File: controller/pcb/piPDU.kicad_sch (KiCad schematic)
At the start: 36 parts, among them J0 SCR_BTN1, J1 SCR_LED1, J10 SCR_BTN6, J11 SCR_LED6, J12 SCR_BTN7, J13 SCR_LED7, J14 SCR_BTN8, J15 SCR_LED8, J16 SCR_BTN9, J17 SCR_LED9, J18 SCR_BTN10, J19 SCR_LED10, J2 SCR_BTN2, J20 SCR_BTN11, J21 SCR_LED11, J22 SCR_BTN12, J23 SCR_LED12, J24 SCR_BTN13, J25 SCR_LED13, J26 SCR_BTN14, J27 SCR_LED14, J28 SCR_BTN15, J29 SCR_LED15, J3 SCR_LED2, J30 SCR_BTN16, J31 SCR_LED16, J32 SCR_5V, J33 SCR_LCD_PWR, J34 SCR_LCD_DATA, J35 Raspberry_Pi_2_3, J4 SCR_BTN3, J5 SCR_LED3, J6 SCR_BTN4, J7 SCR_LED4, J8 SCR_BTN5, J9 SCR_LED5

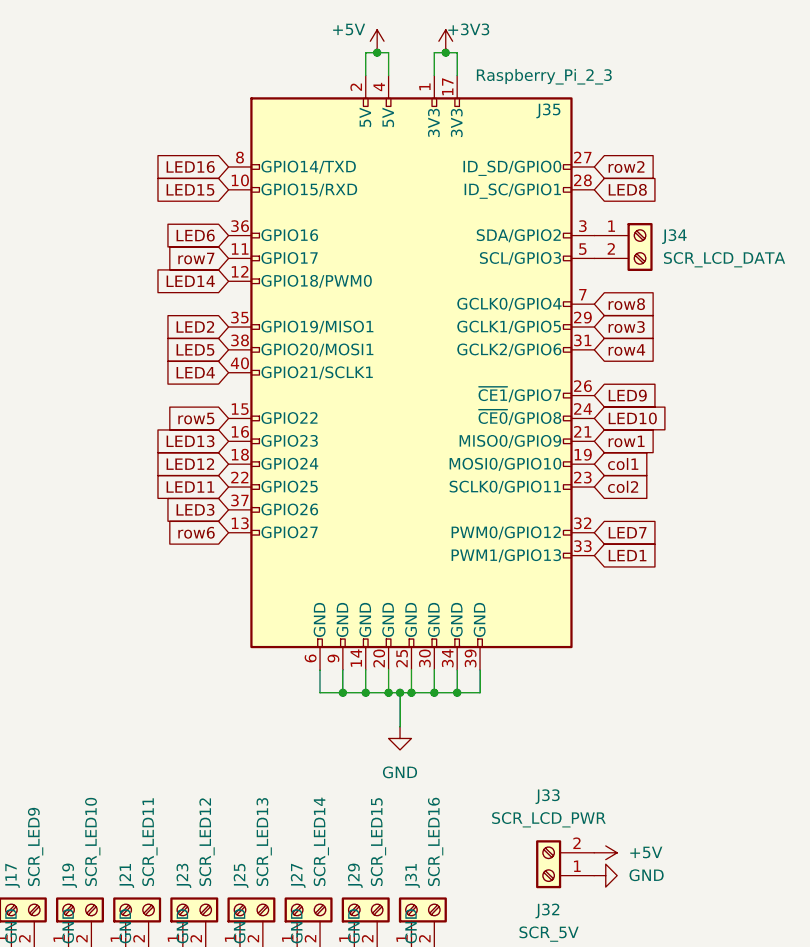
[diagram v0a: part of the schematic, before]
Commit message: Remove redundant connections from the schematic
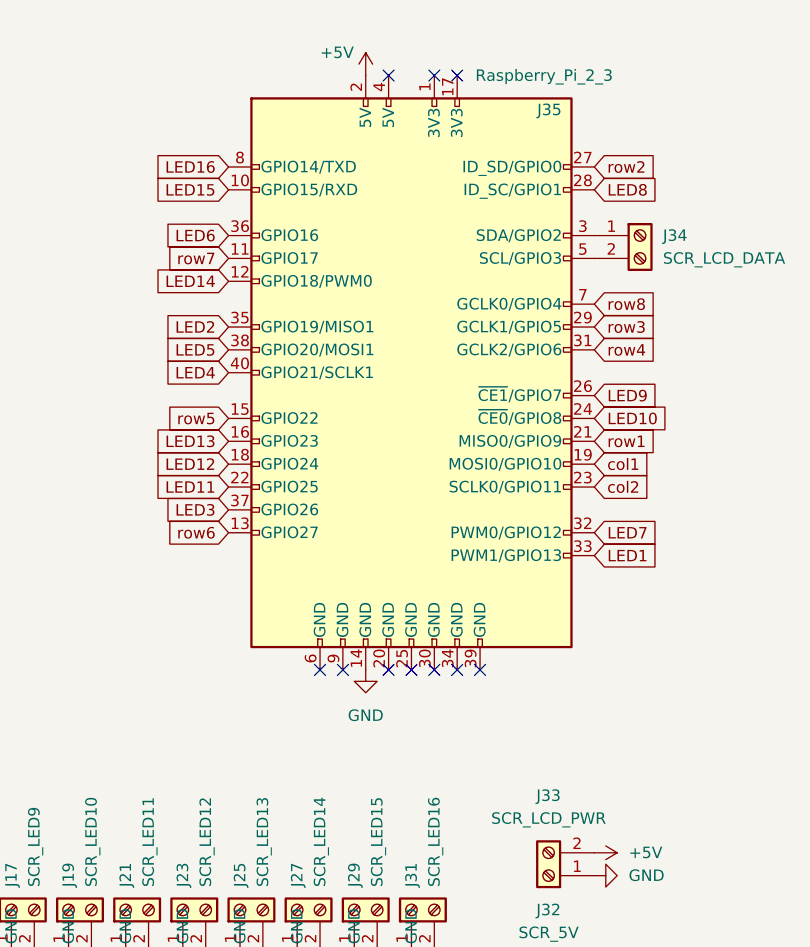
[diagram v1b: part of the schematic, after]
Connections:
- net +5V: no longer J35.4 (5V)
- net GND: no longer J35.20 (GND), J35.25 (GND), J35.30 (GND), J35.34 (GND), J35.39 (GND), J35.6 (GND), J35.9 (GND)
- net +3V3: no longer names the net of J35.1 (3V3)
- net +3V3: no longer J35.17 (3V3)
- no-connect marks 0 -> 10
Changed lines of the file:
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@@
   (junction (at 55.88 69.85) (diameter 0) (color 0 0 0 0)
   )
-  (junction (at 113.03 88.9) (diameter 0) (color 0 0 0 0)
-  )
-  (junction (at 109.22 17.78) (diameter 0) (color 0 0 0 0)
-  )
   (junction (at 55.88 39.37) (diameter 0) (color 0 0 0 0)
   )
-  (junction (at 110.49 88.9) (diameter 0) (color 0 0 0 0)
-  )
-  (junction (at 107.95 88.9) (diameter 0) (color 0 0 0 0)
-  )
-  (junction (at 111.76 88.9) (diameter 0) (color 0 0 0 0)
-  )
   (junction (at 55.88 54.61) (diameter 0) (color 0 0 0 0)
   )
@@
   (junction (at 36.83 77.47) (diameter 0) (color 0 0 0 0)
   )
-  (junction (at 105.41 88.9) (diameter 0) (color 0 0 0 0)
-  )
   (junction (at 54.61 58.42) (diameter 0) (color 0 0 0 0)
   )
   (junction (at 36.83 31.75) (diameter 0) (color 0 0 0 0)
   )
-  (junction (at 115.57 88.9) (diameter 0) (color 0 0 0 0)
-  )
-  (junction (at 116.84 17.78) (diameter 0) (color 0 0 0 0)
-  )
-  (junction (at 118.11 88.9) (diameter 0) (color 0 0 0 0)
-  )
+  (no_connect (at 105.41 86.36))
+  (no_connect (at 118.11 20.32))
+  (no_connect (at 118.11 86.36))
+  (no_connect (at 120.65 86.36))
+  (no_connect (at 115.57 20.32))
+  (no_connect (at 113.03 86.36))
+  (no_connect (at 110.49 86.36))
+  (no_connect (at 115.57 86.36))
+  (no_connect (at 102.87 86.36))
+  (no_connect (at 110.49 20.32))
   (wire (pts (xy 54.61 50.8) (xy 54.61 49.53))
     (stroke (width 0) (type default) (color 0 0 0 0))
@@
     (stroke (width 0) (type default) (color 0 0 0 0))
   )
-  (wire (pts (xy 102.87 86.36) (xy 102.87 88.9))
-    (stroke (width 0) (type default) (color 0 0 0 0))
-  )
-  (wire (pts (xy 115.57 20.32) (xy 115.57 17.78))
-    (stroke (width 0) (type default) (color 0 0 0 0))
-  )
   (wire (pts (xy 36.83 69.85) (xy 35.56 69.85))
     (stroke (width 0) (type default) (color 0 0 0 0))
   )
-  (wire (pts (xy 107.95 17.78) (xy 107.95 20.32))
-    (stroke (width 0) (type default) (color 0 0 0 0))
-  )
-  (wire (pts (xy 115.57 17.78) (xy 116.84 17.78))
-    (stroke (width 0) (type default) (color 0 0 0 0))
-  )
-  (wire (pts (xy 111.76 88.9) (xy 113.03 88.9))
-    (stroke (width 0) (type default) (color 0 0 0 0))
-  )
   (wire (pts (xy 36.83 46.99) (xy 36.83 54.61))
     (stroke (width 0) (type default) (color 0 0 0 0))
   )
-  (wire (pts (xy 107.95 88.9) (xy 110.49 88.9))
-    (stroke (width 0) (type default) (color 0 0 0 0))
-  )
   (wire (pts (xy 57.15 24.13) (xy 55.88 24.13))
     (stroke (width 0) (type default) (color 0 0 0 0))
@@
     (stroke (width 0) (type default) (color 0 0 0 0))
   )
-  (wire (pts (xy 107.95 86.36) (xy 107.95 88.9))
-    (stroke (width 0) (type default) (color 0 0 0 0))
-  )
   (wire (pts (xy 36.83 39.37) (xy 35.56 39.37))
     (stroke (width 0) (type default) (color 0 0 0 0))
@@
     (stroke (width 0) (type default) (color 0 0 0 0))
   )
-  (wire (pts (xy 113.03 86.36) (xy 113.03 88.9))
-    (stroke (width 0) (type default) (color 0 0 0 0))
-  )
-  (wire (pts (xy 118.11 86.36) (xy 118.11 88.9))
-    (stroke (width 0) (type default) (color 0 0 0 0))
-  )
   (wire (pts (xy 54.61 73.66) (xy 58.42 73.66))
     (stroke (width 0) (type default) (color 0 0 0 0))
   )
-  (wire (pts (xy 111.76 88.9) (xy 110.49 88.9))
-    (stroke (width 0) (type default) (color 0 0 0 0))
-  )
   (wire (pts (xy 35.56 87.63) (xy 35.56 90.17))
     (stroke (width 0) (type default) (color 0 0 0 0))
@@
     (stroke (width 0) (type default) (color 0 0 0 0))
   )
-  (wire (pts (xy 118.11 17.78) (xy 118.11 20.32))
-    (stroke (width 0) (type default) (color 0 0 0 0))
-  )
   (wire (pts (xy 55.88 24.13) (xy 55.88 31.75))
     (stroke (width 0) (type default) (color 0 0 0 0))
@@
     (stroke (width 0) (type default) (color 0 0 0 0))
   )
-  (wire (pts (xy 118.11 88.9) (xy 120.65 88.9))
-    (stroke (width 0) (type default) (color 0 0 0 0))
-  )
   (wire (pts (xy 35.56 34.29) (xy 35.56 36.83))
     (stroke (width 0) (type default) (color 0 0 0 0))
   )
-  (wire (pts (xy 105.41 86.36) (xy 105.41 88.9))
-    (stroke (width 0) (type default) (color 0 0 0 0))
-  )
   (wire (pts (xy 35.56 36.83) (xy 54.61 36.83))
     (stroke (width 0) (type default) (color 0 0 0 0))
@@
     (stroke (width 0) (type default) (color 0 0 0 0))
   )
-  (wire (pts (xy 110.49 86.36) (xy 110.49 88.9))
-    (stroke (width 0) (type default) (color 0 0 0 0))
-  )
-  (wire (pts (xy 111.76 92.71) (xy 111.76 88.9))
-    (stroke (width 0) (type default) (color 0 0 0 0))
-  )
   (wire (pts (xy 36.83 31.75) (xy 36.83 39.37))
     (stroke (width 0) (type default) (color 0 0 0 0))
@@
     (stroke (width 0) (type default) (color 0 0 0 0))
   )
-  (wire (pts (xy 115.57 86.36) (xy 115.57 88.9))
-    (stroke (width 0) (type default) (color 0 0 0 0))
-  )
   (wire (pts (xy 35.56 74.93) (xy 54.61 74.93))
     (stroke (width 0) (type default) (color 0 0 0 0))
@@
     (stroke (width 0) (type default) (color 0 0 0 0))
   )
-  (wire (pts (xy 110.49 20.32) (xy 110.49 17.78))
-    (stroke (width 0) (type default) (color 0 0 0 0))
-  )
   (wire (pts (xy 35.56 80.01) (xy 35.56 82.55))
     (stroke (width 0) (type default) (color 0 0 0 0))
@@
     (stroke (width 0) (type default) (color 0 0 0 0))
   )
-  (wire (pts (xy 110.49 17.78) (xy 109.22 17.78))
-    (stroke (width 0) (type default) (color 0 0 0 0))
-  )
   (wire (pts (xy 55.88 77.47) (xy 55.88 85.09))
     (stroke (width 0) (type default) (color 0 0 0 0))
@@
     (stroke (width 0) (type default) (color 0 0 0 0))
   )
-  (wire (pts (xy 116.84 17.78) (xy 118.11 17.78))
-    (stroke (width 0) (type default) (color 0 0 0 0))
-  )
   (wire (pts (xy 36.83 85.09) (xy 35.56 85.09))
     (stroke (width 0) (type default) (color 0 0 0 0))
@@
     (stroke (width 0) (type default) (color 0 0 0 0))
   )
-  (wire (pts (xy 113.03 88.9) (xy 115.57 88.9))
-    (stroke (width 0) (type default) (color 0 0 0 0))
-  )
   (wire (pts (xy 54.61 67.31) (xy 54.61 66.04))
     (stroke (width 0) (type default) (color 0 0 0 0))
@@
     (stroke (width 0) (type default) (color 0 0 0 0))
   )
-  (wire (pts (xy 109.22 17.78) (xy 107.95 17.78))
-    (stroke (width 0) (type default) (color 0 0 0 0))
-  )
   (wire (pts (xy 54.61 77.47) (xy 55.88 77.47))
     (stroke (width 0) (type default) (color 0 0 0 0))
@@
     (stroke (width 0) (type default) (color 0 0 0 0))
   )
-  (wire (pts (xy 120.65 88.9) (xy 120.65 86.36))
-    (stroke (width 0) (type default) (color 0 0 0 0))
-  )
-  (wire (pts (xy 115.57 88.9) (xy 118.11 88.9))
-    (stroke (width 0) (type default) (color 0 0 0 0))
-  )
   (wire (pts (xy 35.56 41.91) (xy 35.56 44.45))
     (stroke (width 0) (type default) (color 0 0 0 0))
@@
     (stroke (width 0) (type default) (color 0 0 0 0))
   )
-  (wire (pts (xy 102.87 88.9) (xy 105.41 88.9))
-    (stroke (width 0) (type default) (color 0 0 0 0))
-  )
   (wire (pts (xy 35.56 57.15) (xy 35.56 59.69))
     (stroke (width 0) (type default) (color 0 0 0 0))
   )
-  (wire (pts (xy 105.41 88.9) (xy 107.95 88.9))
-    (stroke (width 0) (type default) (color 0 0 0 0))
-  )
   (global_label "row5" (shape input) (at 92.71 58.42 180) (fields_autoplaced)
     (effects (font (size 1.27 1.27)) (justify right))
@@
     (pin "2")
   )
-  (symbol (lib_id "power:+5V") (at 109.22 17.78 0) (unit 1)
+  (symbol (lib_id "power:+5V") (at 107.95 20.32 0) (unit 1)
     (in_bom yes) (on_board yes)
-    (property "Reference" "#PWR0121" (id 0) (at 109.22 21.59 0)
-      (effects (font (size 1.27 1.27)) hide)
-    )
-    (property "Value" "+5V" (id 1) (at 104.14 15.24 0)
-      (effects (font (size 1.27 1.27)) (justify left))
-    )
-    (property "Footprint" "" (id 2) (at 109.22 17.78 0)
-      (effects (font (size 1.27 1.27)) hide)
-    )
-    (property "Datasheet" "" (id 3) (at 109.22 17.78 0)
+    (property "Reference" "#PWR0121" (id 0) (at 107.95 24.13 0)
+      (effects (font (size 1.27 1.27)) hide)
+    )
+    (property "Value" "+5V" (id 1) (at 102.87 17.78 0)
+      (effects (font (size 1.27 1.27)) (justify left))
+    )
+    (property "Footprint" "" (id 2) (at 107.95 20.32 0)
+      (effects (font (size 1.27 1.27)) hide)
+    )
+    (property "Datasheet" "" (id 3) (at 107.95 20.32 0)
       (effects (font (size 1.27 1.27)) hide)
     )
@@
     (pin "2")
   )
-  (symbol (lib_id "power:GND") (at 111.76 92.71 0) (unit 1)
-    (in_bom yes) (on_board yes) (fields_autoplaced)
-    (property "Reference" "#PWR0103" (id 0) (at 111.76 99.06 0)
-      (effects (font (size 1.27 1.27)) hide)
-    )
-    (property "Value" "GND" (id 1) (at 111.76 97.79 0))
-    (property "Footprint" "" (id 2) (at 111.76 92.71 0)
-      (effects (font (size 1.27 1.27)) hide)
-    )
-    (property "Datasheet" "" (id 3) (at 111.76 92.71 0)
+  (symbol (lib_id "power:GND") (at 107.95 86.36 0) (unit 1)
+    (in_bom yes) (on_board yes) (fields_autoplaced)
+    (property "Reference" "#PWR0103" (id 0) (at 107.95 92.71 0)
+      (effects (font (size 1.27 1.27)) hide)
+    )
+    (property "Value" "GND" (id 1) (at 107.95 91.44 0))
+    (property "Footprint" "" (id 2) (at 107.95 86.36 0)
+      (effects (font (size 1.27 1.27)) hide)
+    )
+    (property "Datasheet" "" (id 3) (at 107.95 86.36 0)
       (effects (font (size 1.27 1.27)) hide)
     )
@@
     (pin "1")
     (pin "2")
-  )
-  (symbol (lib_id "power:+3V3") (at 116.84 17.78 0) (unit 1)
-    (in_bom yes) (on_board yes)
-    (property "Reference" "#PWR0127" (id 0) (at 116.84 21.59 0)
-      (effects (font (size 1.27 1.27)) hide)
-    )
-    (property "Value" "+3V3" (id 1) (at 119.38 15.24 0))
-    (property "Footprint" "" (id 2) (at 116.84 17.78 0)
-      (effects (font (size 1.27 1.27)) hide)
-    )
-    (property "Datasheet" "" (id 3) (at 116.84 17.78 0)
-      (effects (font (size 1.27 1.27)) hide)
-    )
-    (pin "1")
   )
   (symbol (lib_id "Connector:Screw_Terminal_01x02") (at 30.48 87.63 180) (unit 1)
@@
       (reference "#PWR0123") (unit 1) (value "+5V") (footprint "")
     )
-    (path "/de3aaaf3-a39e-4cbf-8204-ff4e2ed5a356"
-      (reference "#PWR0127") (unit 1) (value "+3V3") (footprint "")
-    )
     (path "/676515b6-e10e-4a3a-b318-3969763a4732"

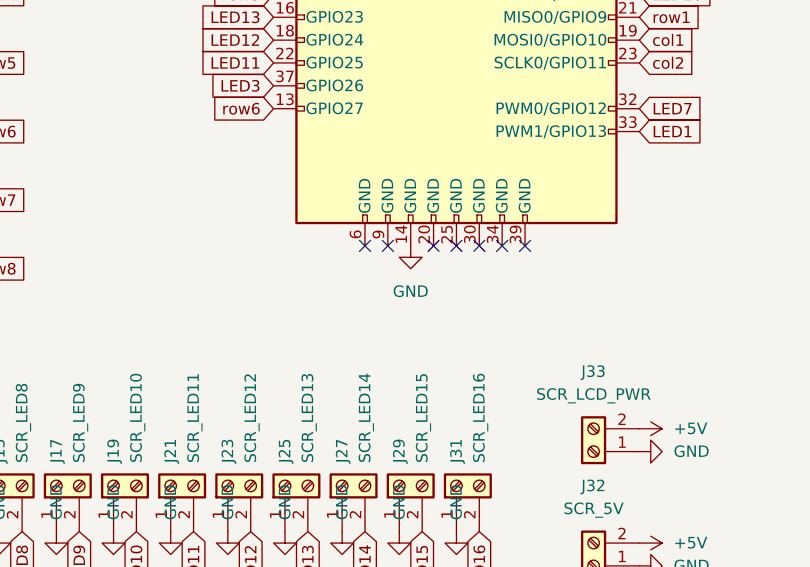
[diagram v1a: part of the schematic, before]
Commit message: Fix PCB and schematic redundant connections
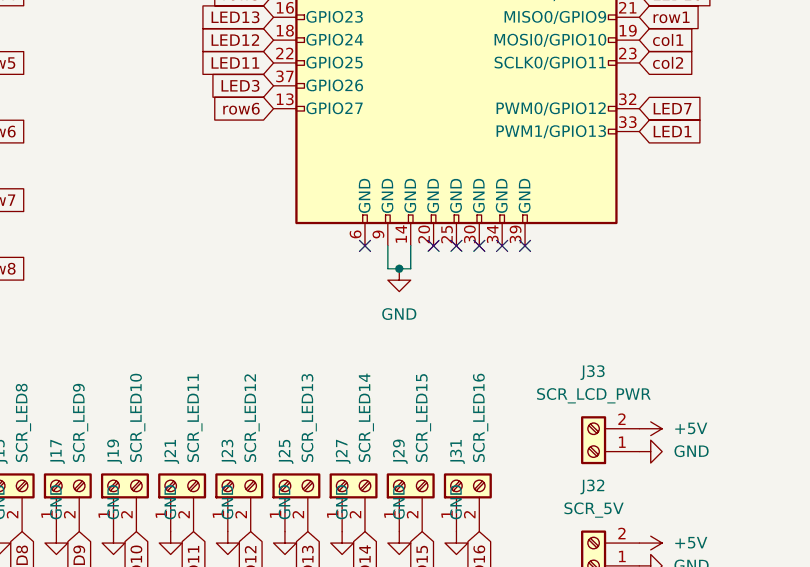
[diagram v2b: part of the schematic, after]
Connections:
- net GND: now also J35.9 (GND)
- no-connect marks 10 -> 9
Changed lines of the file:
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@@
   (junction (at 55.88 62.23) (diameter 0) (color 0 0 0 0)
   )
+  (junction (at 106.68 88.9) (diameter 0) (color 0 0 0 0)
+  )
   (junction (at 54.61 73.66) (diameter 0) (color 0 0 0 0)
   )
@@
   (junction (at 36.83 31.75) (diameter 0) (color 0 0 0 0)
   )
-  (no_connect (at 105.41 86.36))
   (no_connect (at 118.11 20.32))
   (no_connect (at 118.11 86.36))
@@
     (stroke (width 0) (type default) (color 0 0 0 0))
   )
+  (wire (pts (xy 105.41 86.36) (xy 105.41 88.9))
+    (stroke (width 0) (type default) (color 0 0 0 0))
+  )
   (wire (pts (xy 57.15 24.13) (xy 55.88 24.13))
     (stroke (width 0) (type default) (color 0 0 0 0))
@@
     (stroke (width 0) (type default) (color 0 0 0 0))
   )
+  (wire (pts (xy 107.95 88.9) (xy 106.68 88.9))
+    (stroke (width 0) (type default) (color 0 0 0 0))
+  )
+  (wire (pts (xy 105.41 88.9) (xy 106.68 88.9))
+    (stroke (width 0) (type default) (color 0 0 0 0))
+  )
   (wire (pts (xy 55.88 85.09) (xy 54.61 85.09))
     (stroke (width 0) (type default) (color 0 0 0 0))
@@
   )
   (wire (pts (xy 54.61 39.37) (xy 55.88 39.37))
+    (stroke (width 0) (type default) (color 0 0 0 0))
+  )
+  (wire (pts (xy 107.95 86.36) (xy 107.95 88.9))
     (stroke (width 0) (type default) (color 0 0 0 0))
   )
@@
     (pin "2")
   )
-  (symbol (lib_id "power:GND") (at 107.95 86.36 0) (unit 1)
-    (in_bom yes) (on_board yes) (fields_autoplaced)
-    (property "Reference" "#PWR0103" (id 0) (at 107.95 92.71 0)
-      (effects (font (size 1.27 1.27)) hide)
-    )
-    (property "Value" "GND" (id 1) (at 107.95 91.44 0))
-    (property "Footprint" "" (id 2) (at 107.95 86.36 0)
-      (effects (font (size 1.27 1.27)) hide)
-    )
-    (property "Datasheet" "" (id 3) (at 107.95 86.36 0)
-      (effects (font (size 1.27 1.27)) hide)
-    )
+  (symbol (lib_id "power:GND") (at 106.68 88.9 0) (unit 1)
+    (in_bom yes) (on_board yes) (fields_autoplaced)
+    (property "Reference" "#PWR0103" (id 0) (at 106.68 95.25 0)
+      (effects (font (size 1.27 1.27)) hide)
+    )
+    (property "Value" "GND" (id 1) (at 106.68 93.98 0))
+    (property "Footprint" "" (id 2) (at 106.68 88.9 0)
+      (effects (font (size 1.27 1.27)) hide)
+    )
+    (property "Datasheet" "" (id 3) (at 106.68 88.9 0)
+      (effects (font (size 1.27 1.27)) hide)
+    )

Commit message: Make tracks thicker and more spaced out
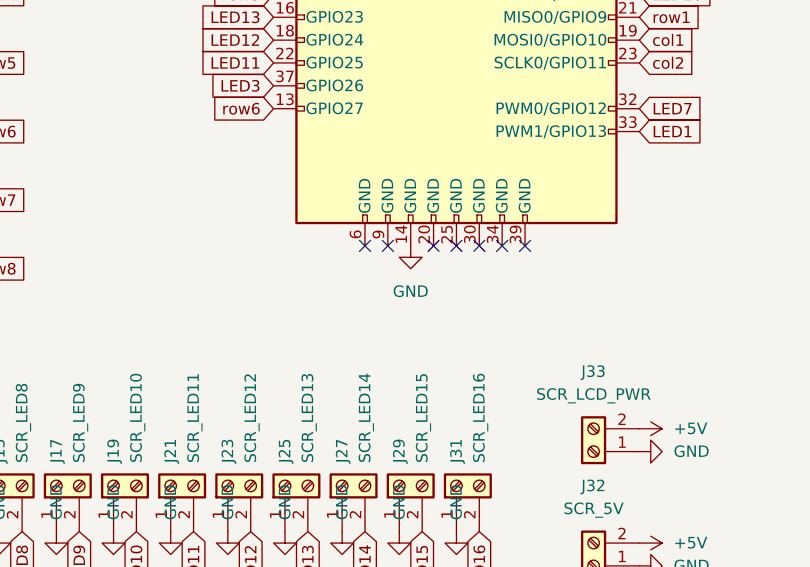
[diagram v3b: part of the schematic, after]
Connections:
- net GND: no longer J35.9 (GND)
- no-connect marks 9 -> 10
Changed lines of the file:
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@@
   (junction (at 55.88 62.23) (diameter 0) (color 0 0 0 0)
-  )
-  (junction (at 106.68 88.9) (diameter 0) (color 0 0 0 0)
   )
   (junction (at 54.61 73.66) (diameter 0) (color 0 0 0 0)
@@
   (no_connect (at 102.87 86.36))
   (no_connect (at 110.49 20.32))
+  (no_connect (at 105.41 86.36))
   (wire (pts (xy 54.61 50.8) (xy 54.61 49.53))
     (stroke (width 0) (type default) (color 0 0 0 0))
@@
     (stroke (width 0) (type default) (color 0 0 0 0))
   )
-  (wire (pts (xy 105.41 86.36) (xy 105.41 88.9))
-    (stroke (width 0) (type default) (color 0 0 0 0))
-  )
   (wire (pts (xy 57.15 24.13) (xy 55.88 24.13))
     (stroke (width 0) (type default) (color 0 0 0 0))
@@
     (stroke (width 0) (type default) (color 0 0 0 0))
   )
-  (wire (pts (xy 107.95 88.9) (xy 106.68 88.9))
-    (stroke (width 0) (type default) (color 0 0 0 0))
-  )
-  (wire (pts (xy 105.41 88.9) (xy 106.68 88.9))
-    (stroke (width 0) (type default) (color 0 0 0 0))
-  )
   (wire (pts (xy 55.88 85.09) (xy 54.61 85.09))
     (stroke (width 0) (type default) (color 0 0 0 0))
@@
   )
   (wire (pts (xy 54.61 39.37) (xy 55.88 39.37))
-    (stroke (width 0) (type default) (color 0 0 0 0))
-  )
-  (wire (pts (xy 107.95 86.36) (xy 107.95 88.9))
     (stroke (width 0) (type default) (color 0 0 0 0))
   )
@@
     (pin "2")
   )
-  (symbol (lib_id "power:GND") (at 106.68 88.9 0) (unit 1)
-    (in_bom yes) (on_board yes) (fields_autoplaced)
-    (property "Reference" "#PWR0103" (id 0) (at 106.68 95.25 0)
-      (effects (font (size 1.27 1.27)) hide)
-    )
-    (property "Value" "GND" (id 1) (at 106.68 93.98 0))
-    (property "Footprint" "" (id 2) (at 106.68 88.9 0)
-      (effects (font (size 1.27 1.27)) hide)
-    )
-    (property "Datasheet" "" (id 3) (at 106.68 88.9 0)
-      (effects (font (size 1.27 1.27)) hide)
-    )
+  (symbol (lib_id "power:GND") (at 107.95 86.36 0) (unit 1)
+    (in_bom yes) (on_board yes) (fields_autoplaced)
+    (property "Reference" "#PWR0103" (id 0) (at 107.95 92.71 0)
+      (effects (font (size 1.27 1.27)) hide)
+    )
+    (property "Value" "GND" (id 1) (at 107.95 91.44 0))
+    (property "Footprint" "" (id 2) (at 107.95 86.36 0)
+      (effects (font (size 1.27 1.27)) hide)
+    )
+    (property "Datasheet" "" (id 3) (at 107.95 86.36 0)
+      (effects (font (size 1.27 1.27)) hide)
+    )
